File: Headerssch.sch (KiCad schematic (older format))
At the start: 20 parts, among them J18 GPS, J19 Radio, J20 Recovery, J21 Propulsion, J22 Tank Pressure, J23 Low Pressure, J24 Conn_01x06, J25 Battery, J26 Launch Systems, J27 SD

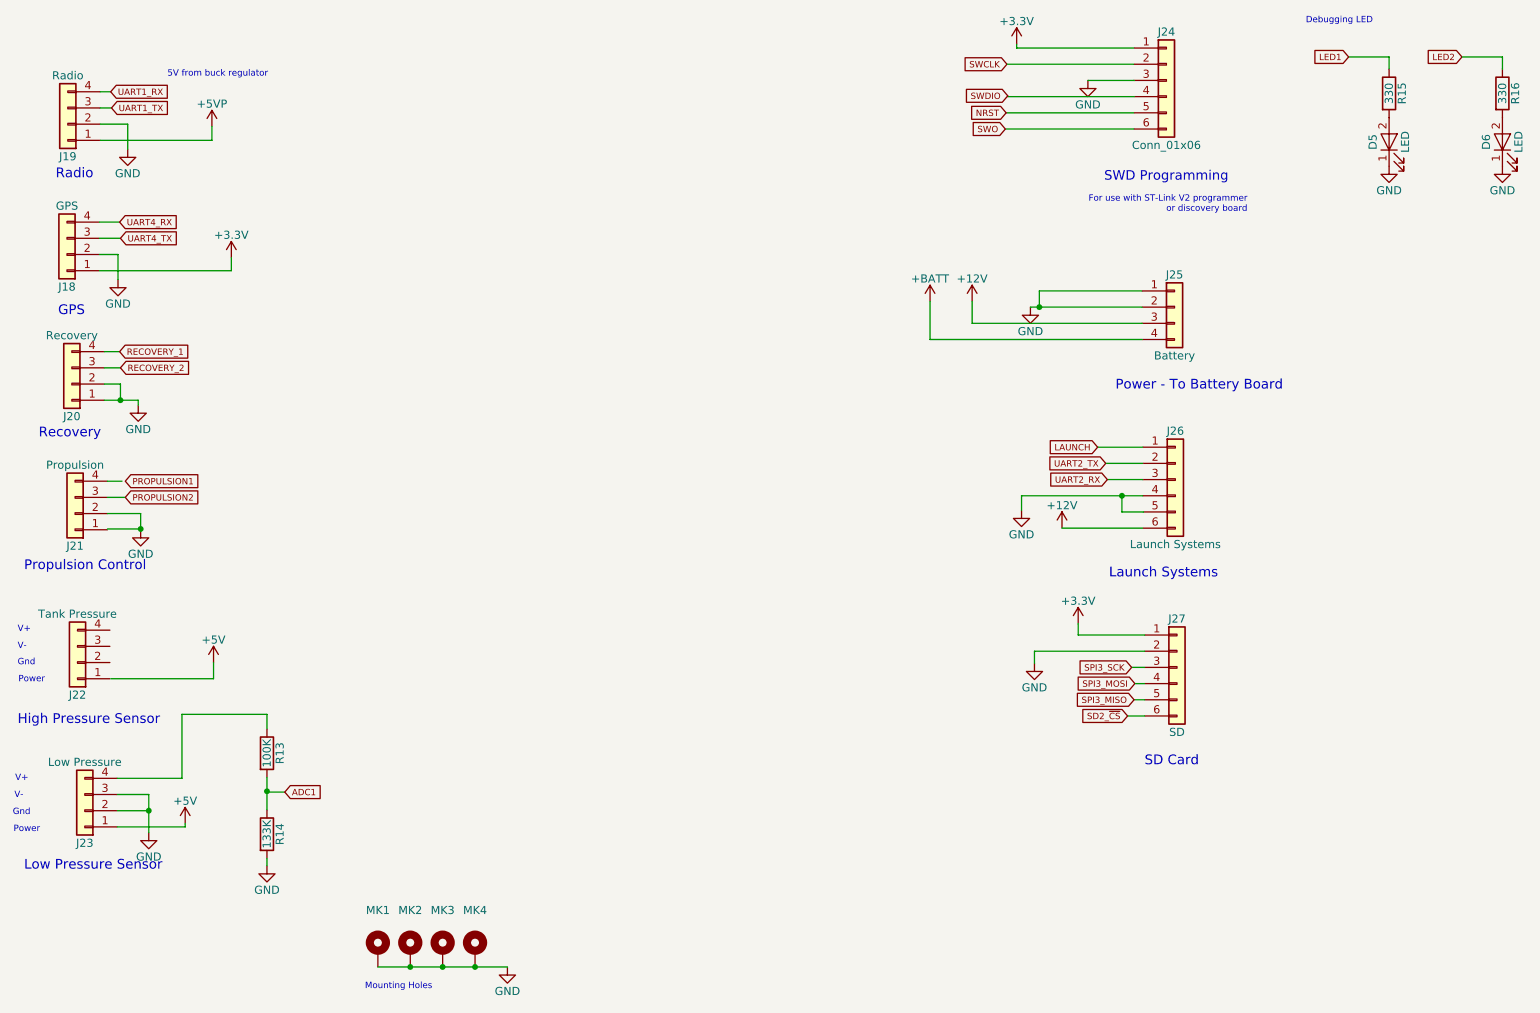
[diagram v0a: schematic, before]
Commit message: Bring schematic in line with PCB. Previous update broke this.
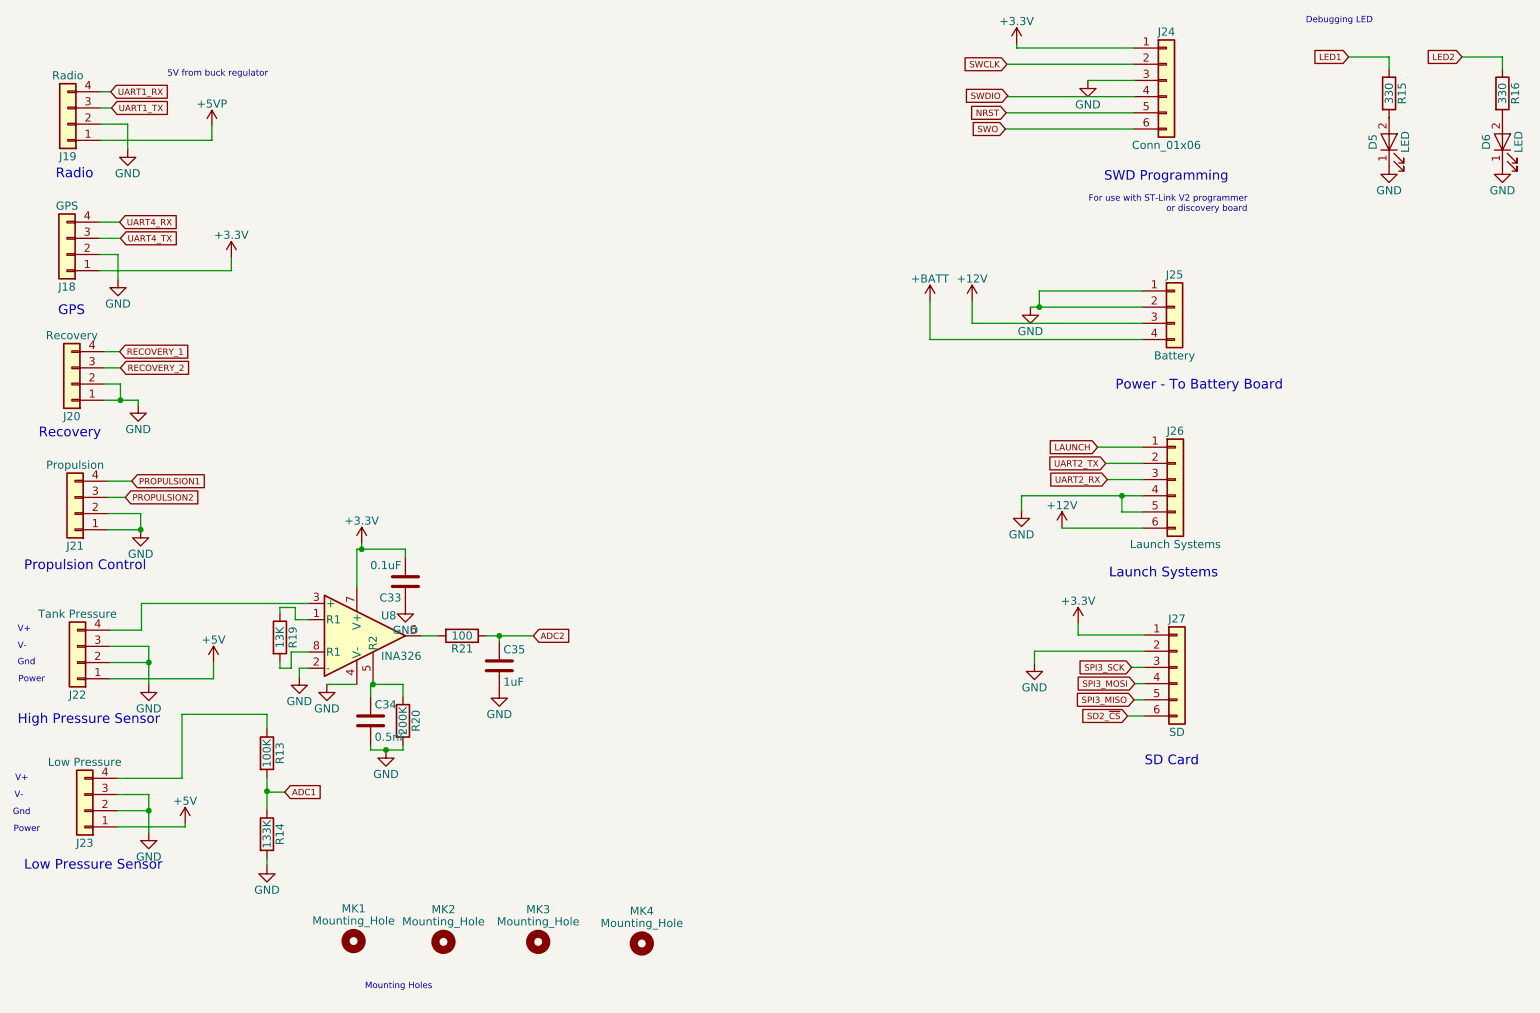
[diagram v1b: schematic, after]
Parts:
- removed MK1, MK2, MK3, MK4: Mounting_Hole_PAD, MountingHole:MountingHole_3.2mm_M3_Pad, symbol Mounting_Hole_PAD
- added C33: 0.1uF, Capacitors_SMD:C_0603, symbol C
- added C34: 0.5nF, Capacitors_SMD:C_0603, symbol C
- added C35: 1uF, Capacitors_SMD:C_0603, symbol C
- added MK1, MK2, MK3, MK4: Mounting_Hole, Mounting_Holes:MountingHole_3.2mm_M3, symbol Mounting_Hole
- added R19: 13K, Resistors_SMD:R_0603, symbol R
- added R20: 200K, Resistors_SMD:R_0603, symbol R
- added R21: 100, Resistors_SMD:R_0603, symbol R
- added U8: INA326, Housings_SSOP:MSOP-8_3x3mm_Pitch0.65mm, symbol INA326
- R13, R14: footprint (none) -> Resistors_SMD:R_0603
- R15, R16: footprint Resistor_SMD:R_0603_1608Metric -> Resistors_SMD:R_0603
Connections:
- net labels added: ADC2
- wire segments 74 -> 103

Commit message: Add schem documentation and generate new PDF
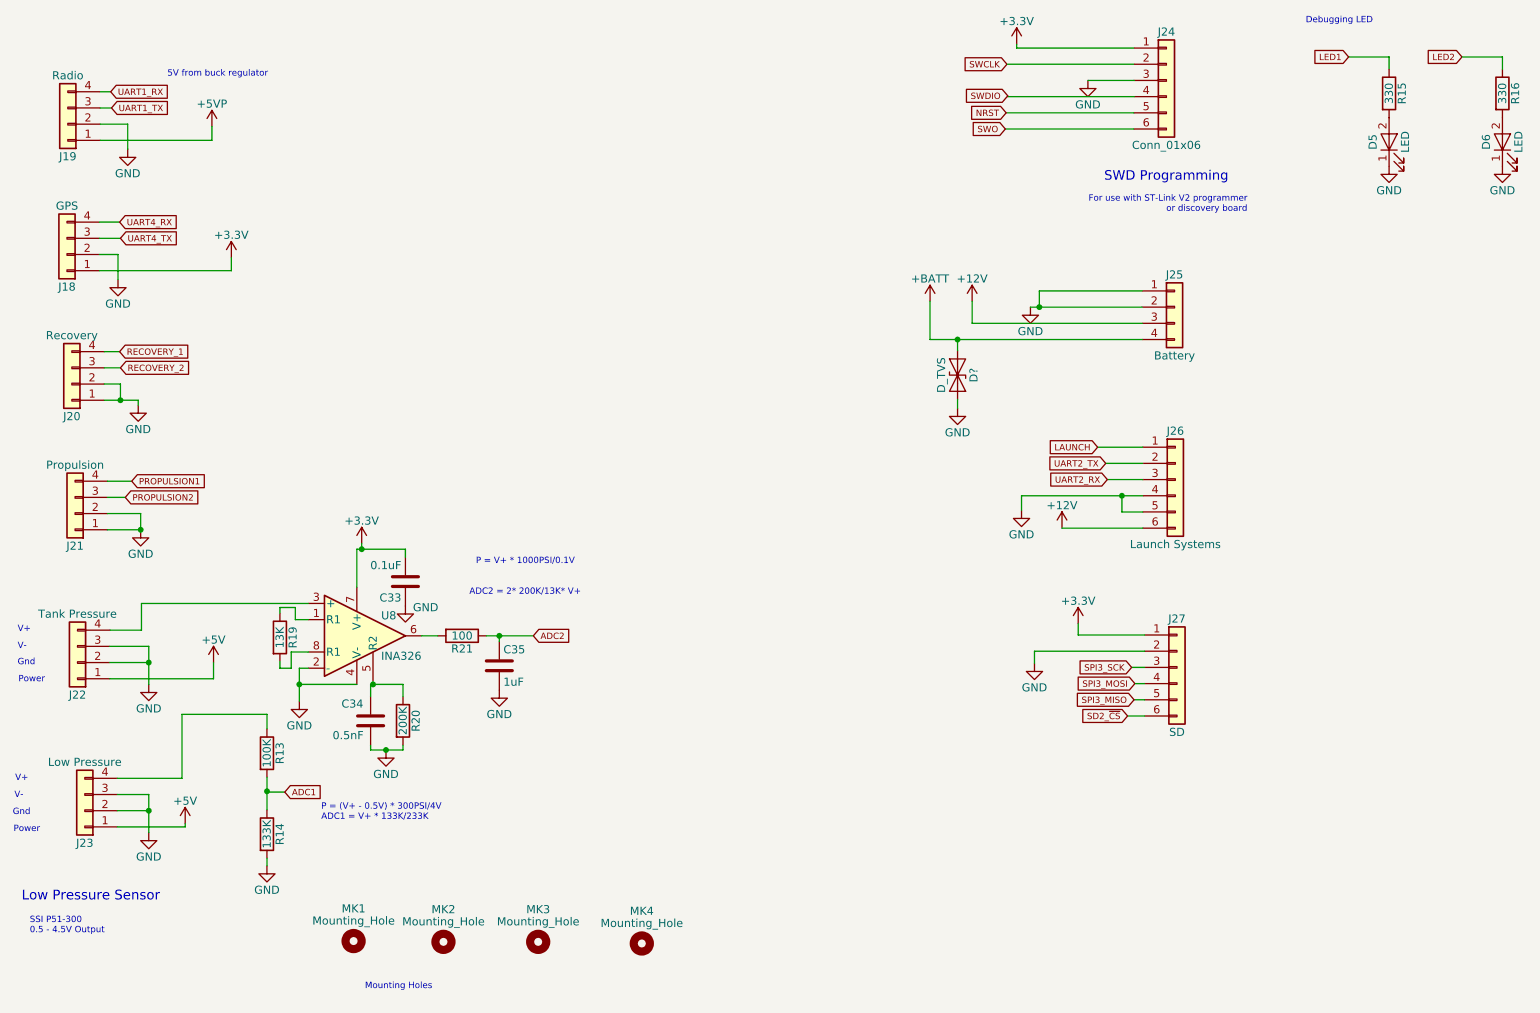
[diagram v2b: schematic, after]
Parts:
- added D?: D_TVS, symbol D_TVS
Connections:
- net +BATT: now also D?.1 (A1)
- net GND: now also D?.2 (A2)
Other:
- note added: "ADC2 = 2* 200K/13K* V+"
- note added: "P = (V+ - 0.5V) * 300PSI/4V\nADC1 = V+ * 133K/233K"
- note added: "P = V+ * 1000PSI/0.1V"
- note added: "SSI P51-300\n0.5 - 4.5V Output"
- note removed: "GPS"
- note removed: "High Pressure Sensor"
- note removed: "Launch Systems"
- note removed: "Power - To Battery Board"
- note removed: "Propulsion Control"
- note removed: "Radio"
- note removed: "Recovery"
- note removed: "SD Card"
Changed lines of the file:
@@
 	-1   0    0    1
 $EndComp
-Text Notes 1010 1840 0    60   ~ 0
-Radio
 $Comp
 L Conn_01x04 J18
@@
 	-1   0    0    1
 $EndComp
-Text Notes 1025 2685 0    60   ~ 0
-GPS
 $Comp
 L Conn_01x04 J20
@@
 	-1   0    0    1
 $EndComp
-Text Notes 815  4260 0    60   ~ 0
-Propulsion Control
 $Comp
 L Conn_01x04 J21
@@
 	-1   0    0    1
 $EndComp
-Text Notes 775  5210 0    60   ~ 0
-High Pressure Sensor
 $Comp
 L Conn_01x04 J23
@@
 	-1   0    0    1
 $EndComp
-Text Notes 815  6110 0    60   ~ 0
+Text Notes 800  6300 0    60   ~ 0
 Low Pressure Sensor
-Text Notes 7515 4305 0    60   ~ 0
-Launch Systems
 $Comp
 L Conn_01x06 J27
@@
 	1    0    0    -1
 $EndComp
-Text Notes 7735 5465 0    60   ~ 0
-SD Card
 $Comp
 L Conn_01x04 J25
@@
 	1    0    0    -1
 $EndComp
-Text Notes 7555 3145 0    60   ~ 0
-Power - To Battery Board
 Text GLabel 6875 1525 0    39   Input ~ 0
 SWO
@@
 	1    0    0    -1
 $EndComp
-Text Notes 905  3440 0    60   ~ 0
-Recovery
 Text Notes 780  4950 0    39   ~ 0
 Power
@@
 P 3170 4470
 F 0 "#PWR071" H 3170 4220 50  0001 C CNN
-F 1 "GND" H 3170 4320 50  0000 C CNN
+F 1 "GND" H 3295 4460 50  0000 C CNN
 F 2 "" H 3170 4470 50  0001 C CNN
 F 3 "" H 3170 4470 50  0001 C CNN
@@
 L GND #PWR075
 U 1 1 5AF171BE
-P 2515 4910
-F 0 "#PWR075" H 2515 4660 50  0001 C CNN
-F 1 "GND" H 2515 4760 50  0000 C CNN
-F 2 "" H 2515 4910 50  0001 C CNN
-F 3 "" H 2515 4910 50  0001 C CNN
-	1    2515 4910
+P 2515 5060
+F 0 "#PWR075" H 2515 4810 50  0001 C CNN
+F 1 "GND" H 2515 4910 50  0000 C CNN
+F 2 "" H 2515 5060 50  0001 C CNN
+F 3 "" H 2515 5060 50  0001 C CNN
+	1    2515 5060
 	1    0    0    -1
 $EndComp
@@
 	1    0    0    -1
 $EndComp
-$Comp
-L GND #PWR077
-U 1 1 5AF17BF2
-P 2685 4955
-F 0 "#PWR077" H 2685 4705 50  0001 C CNN
-F 1 "GND" H 2685 4805 50  0000 C CNN
-F 2 "" H 2685 4955 50  0001 C CNN
-F 3 "" H 2685 4955 50  0001 C CNN
-	1    2685 4955
-	1    0    0    -1
-$EndComp
-Wire Wire Line
-	2870 4955 2685 4955
 Connection ~ 1585 4820
 Wire Wire Line
@@
 	2570 4455 1540 4455
 Wire Wire Line
-	2515 4855 2515 4910
+	2515 4855 2515 5060
 Wire Wire Line
 	2570 4855 2515 4855
@@
 U 1 1 5AF1AA5A
 P 2955 5180
-F 0 "C34" H 2980 5280 50  0000 L CNN
-F 1 "0.5nF" H 2980 5080 50  0000 L CNN
+F 0 "C34" H 2775 5285 50  0000 L CNN
+F 1 "0.5nF" H 2720 5090 50  0000 L CNN
 F 2 "Capacitors_SMD:C_0603" H 2993 5030 50  0001 C CNN
 F 3 "" H 2955 5180 50  0001 C CNN
@@
 	3155 5360 3155 5330
 Connection ~ 3050 5360
+Text Notes 850  6500 0    39   ~ 0
+SSI P51-300\n0.5 - 4.5V Output
+Text Notes 2650 5800 0    39   ~ 0
+P = (V+ - 0.5V) * 300PSI/4V\nADC1 = V+ * 133K/233K
+Wire Wire Line
+	2515 4955 2870 4955
+Connection ~ 2515 4955
+Text Notes 3565 4410 0    39   ~ 0
+ADC2 = 2* 200K/13K* V+
+Text Notes 3605 4220 0    39   ~ 0
+P = V+ * 1000PSI/0.1V
+$Comp
+L D_TVS D?
+U 1 1 5AF20F24
+P 6580 3045
+F 0 "D?" H 6580 3145 50  0000 C CNN
+F 1 "D_TVS" H 6580 2945 50  0000 C CNN
+F 2 "" H 6580 3045 50  0001 C CNN
+F 3 "" H 6580 3045 50  0001 C CNN
+	1    6580 3045
+	0    1    1    0
+$EndComp
+Wire Wire Line
+	6580 2895 6580 2825
+Connection ~ 6580 2825
+$Comp
+L GND #PWR?
+U 1 1 5AF211F1
+P 6580 3250
+F 0 "#PWR?" H 6580 3000 50  0001 C CNN
+F 1 "GND" H 6580 3100 50  0000 C CNN
+F 2 "" H 6580 3250 50  0001 C CNN
+F 3 "" H 6580 3250 50  0001 C CNN
+	1    6580 3250
+	1    0    0    -1
+$EndComp
+Wire Wire Line
+	6580 3195 6580 3250
 $EndSCHEMATC

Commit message: Changes based on review reccommemdations
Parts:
- added C37: 10u, Capacitors_SMD:C_0603, symbol C
- added R22: 10K, Resistors_SMD:R_0603, symbol R
- D7: renamed from D?; footprint (none) -> Diodes_SMD:D_SOD-323
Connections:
- net +12V: now also D7.1 (A1)
- net +3V3: now also C37.1, R22.1
- net +BATT: no longer D7.1 (A1)
- net GND: now also C37.2
- net SD2_~CS: now also R22.2
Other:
- moved on the sheet: D7
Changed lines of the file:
@@
 Text GLabel 7670 5050 0    39   Input ~ 0
 SPI3_MISO
-Text GLabel 7630 5150 0    39   Input ~ 0
+Text GLabel 6645 5150 0    39   Input ~ 0
 SD2_~CS
 Text GLabel 1405 2900 2    39   Input ~ 0
@@
 	7735 4750 7055 4750
 Wire Wire Line
-	7325 4650 7325 4580
-Wire Wire Line
-	7735 4650 7325 4650
-Wire Wire Line
-	7735 5150 7630 5150
+	7325 4580 7325 4650
+Wire Wire Line
+	7325 4650 7735 4650
+Wire Wire Line
+	6645 5150 7735 5150
 Wire Wire Line
 	7735 5050 7670 5050
@@
 	6410 2825 6410 2590
 Wire Wire Line
-	7720 2825 6410 2825
+	6410 2825 7720 2825
 Wire Wire Line
 	6670 2725 6670 2590
@@
 P = V+ * 1000PSI/0.1V
 $Comp
-L D_TVS D?
+L D_TVS D7
 U 1 1 5AF20F24
-P 6580 3045
-F 0 "D?" H 6580 3145 50  0000 C CNN
-F 1 "D_TVS" H 6580 2945 50  0000 C CNN
-F 2 "" H 6580 3045 50  0001 C CNN
-F 3 "" H 6580 3045 50  0001 C CNN
-	1    6580 3045
+P 7515 4190
+F 0 "D7" H 7515 4290 50  0000 C CNN
+F 1 "D_TVS" H 7515 4090 50  0000 C CNN
+F 2 "Diodes_SMD:D_SOD-323" H 7515 4190 50  0001 C CNN
+F 3 "" H 7515 4190 50  0001 C CNN
+	1    7515 4190
 	0    1    1    0
 $EndComp
@@
 Connection ~ 6580 2825
 $Comp
-L GND #PWR?
+L GND #PWR077
 U 1 1 5AF211F1
-P 6580 3250
-F 0 "#PWR?" H 6580 3000 50  0001 C CNN
-F 1 "GND" H 6580 3100 50  0000 C CNN
-F 2 "" H 6580 3250 50  0001 C CNN
-F 3 "" H 6580 3250 50  0001 C CNN
-	1    6580 3250
-	1    0    0    -1
-$EndComp
-Wire Wire Line
-	6580 3195 6580 3250
+P 7515 4380
+F 0 "#PWR077" H 7515 4130 50  0001 C CNN
+F 1 "GND" H 7515 4230 50  0000 C CNN
+F 2 "" H 7515 4380 50  0001 C CNN
+F 3 "" H 7515 4380 50  0001 C CNN
+	1    7515 4380
+	1    0    0    -1
+$EndComp
+$Comp
+L R R22
+U 1 1 5AF5BB45
+P 6850 4820
+F 0 "R22" V 6930 4820 50  0000 C CNN
+F 1 "10K" V 6850 4820 50  0000 C CNN
+F 2 "Resistors_SMD:R_0603" V 6780 4820 50  0001 C CNN
+F 3 "" H 6850 4820 50  0001 C CNN
+	1    6850 4820
+	1    0    0    -1
+$EndComp
+Wire Wire Line
+	6850 4970 6850 5150
+Connection ~ 6850 5150
+Wire Wire Line
+	6850 4670 6850 4605
+Wire Wire Line
+	6455 4605 7325 4605
+Connection ~ 7325 4605
+$Comp
+L C C37
+U 1 1 5AF5C172
+P 6455 4775
+F 0 "C37" H 6480 4875 50  0000 L CNN
+F 1 "10u" H 6480 4675 50  0000 L CNN
+F 2 "Capacitors_SMD:C_0603" H 6493 4625 50  0001 C CNN
+F 3 "" H 6455 4775 50  0001 C CNN
+	1    6455 4775
+	1    0    0    -1
+$EndComp
+Wire Wire Line
+	6455 4605 6455 4625
+Connection ~ 6850 4605
+$Comp
+L GND #PWR078
+U 1 1 5AF5C431
+P 6455 4940
+F 0 "#PWR078" H 6455 4690 50  0001 C CNN
+F 1 "GND" H 6340 4920 50  0000 C CNN
+F 2 "" H 6455 4940 50  0001 C CNN
+F 3 "" H 6455 4940 50  0001 C CNN
+	1    6455 4940
+	1    0    0    -1
+$EndComp
+Wire Wire Line
+	6455 4925 6455 4940
+Wire Wire Line
+	7515 3990 7515 4040
+Connection ~ 7515 3990
+Wire Wire Line
+	7515 4340 7515 4380
 $EndSCHEMATC

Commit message: Final design published. Gerbers and PDF schematic generated
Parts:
- J18, J19, J20, J21, J22, J23, J25: footprint SOAR_Library:Molex_Micro-Fit_3.0_43045-0400_2x02_P3.00mm_Horizontal -> SOAR_Kicad_Library:Molex_Micro-Fit_3.0_43045-0400_2x02_P3.00mm_Horizontal
- J26, J27: footprint SOAR_Library:Molex_Micro-Fit_3.0_43045-0600_2x03_P3.00mm_Horizontal -> SOAR_Kicad_Library:Molex_Micro-Fit_3.0_43045-0600_2x03_P3.00mm_Horizontal
